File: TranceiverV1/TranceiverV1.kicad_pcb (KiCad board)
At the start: 2 copper layers, 2 parts, among them J1 Conn_01x02_Socket, U1 ESP32-WROOM-32E

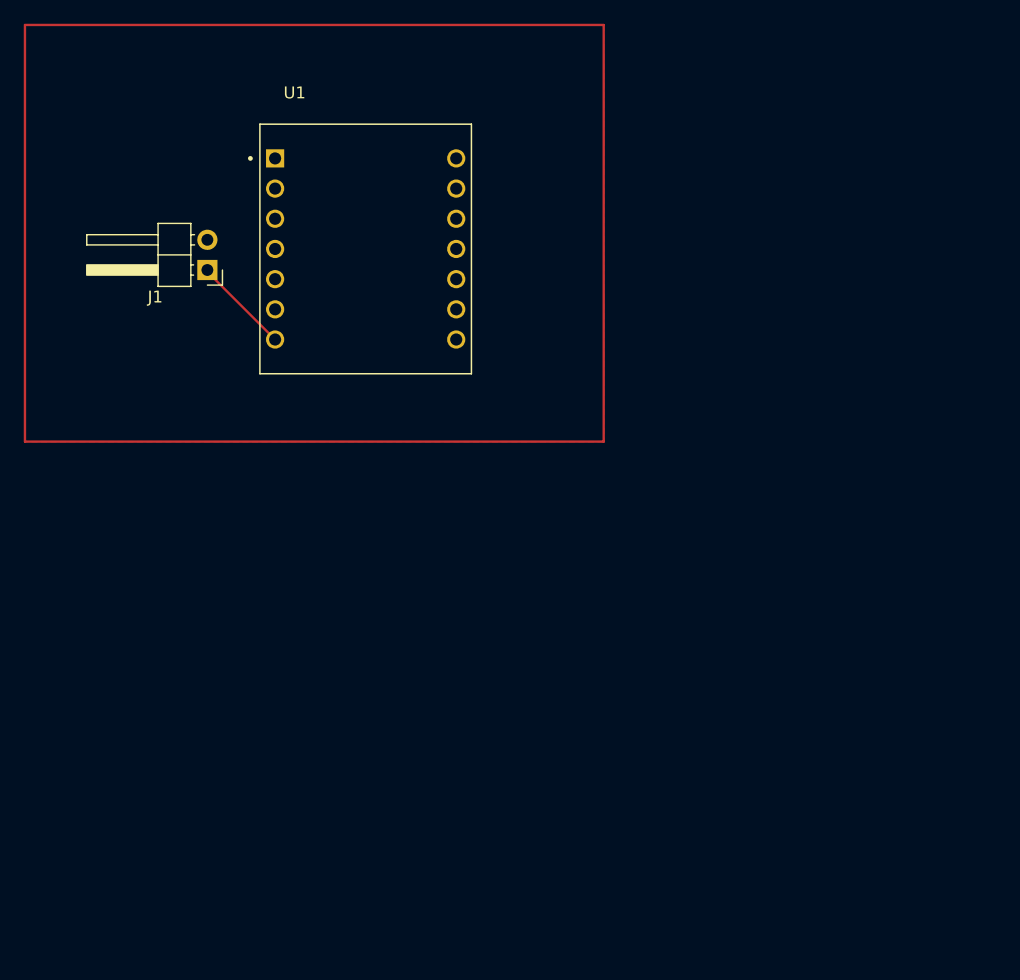
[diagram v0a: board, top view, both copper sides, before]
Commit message: arduino XIAO footprint and symbol added
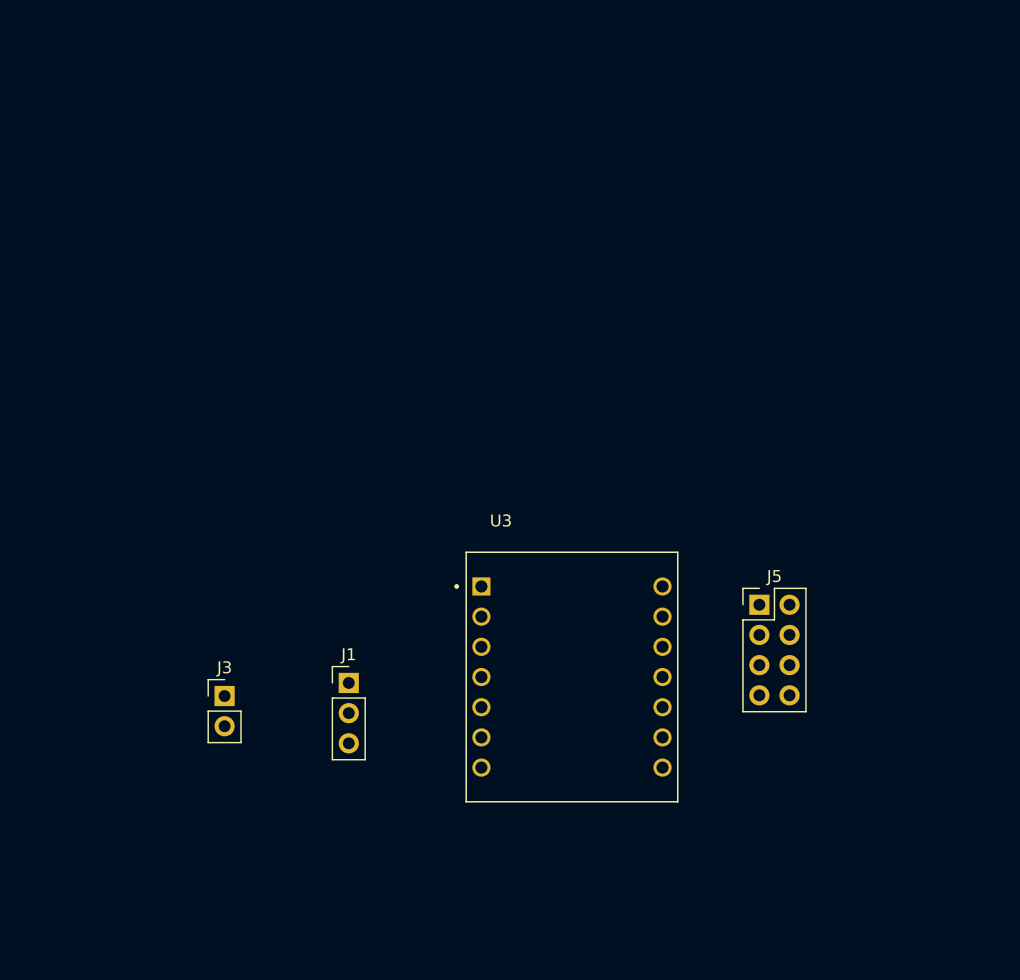
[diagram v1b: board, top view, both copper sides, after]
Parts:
- removed U1: ESP32-WROOM-32E, ArduinoXIAO:MODULE_102010388
- added J3: Conn_01x02_Socket, Connector_PinHeader_2.54mm:PinHeader_1x02_P2.54mm_Vertical, F.Cu at (144.7, 126.6)
- added J5: Conn_02x04_Odd_Even, Connector_PinHeader_2.54mm:PinHeader_2x04_P2.54mm_Vertical, F.Cu at (189.7, 118.9)
- added U3: 102010388, ArduinoXIAO:MODULE_102010388, F.Cu at (174.0, 125.0)
- J1: value Conn_01x02_Socket -> Conn_01x03_Socket; footprint Connector_PinHeader_2.54mm:PinHeader_1x02_P2.54mm_Horizontal -> Connector_PinHeader_2.54mm:PinHeader_1x03_P2.54mm_Vertical
- moved J1 36.7 mm to (155.2, 125.5), turned to 0 degrees
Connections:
- J1 pad 1: Net-(J1-Pin_1) -> /SERVO_DATA
- J1 pad 2: GND -> Net-(J1-Pin_2)
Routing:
- net Net-(J1-Pin_1): track 8.21 -> 0.00 mm
- removed copper zone on F.Cu, net GND

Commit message: designed first iteration of pcb
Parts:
- moved J3 6.16 mm to (150.4, 124.2)
- moved J1 4.72 mm to (158.0, 121.7)
- moved J5 3.49 mm to (192.3, 121.3)
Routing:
- net /CE: track 0.00 -> 45.4 mm, vias 0 -> 1
- net /CS: track 0.00 -> 45.1 mm
- net /VCC: track 0.00 -> 35.2 mm
- net /MOSI: track 0.00 -> 32.2 mm, vias 0 -> 1
- net /MISO: track 0.00 -> 26.6 mm
- net /SCK: track 0.00 -> 12.2 mm
- net /SERVO_DATA: track 0.00 -> 11.9 mm
- net GND: track 0.00 -> 11.3 mm
- net Net-(J1-Pin_2): track 0.00 -> 7.61 mm
- added copper zone on B.Cu, net GND
- added copper zone on F.Cu, net GND
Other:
- board outline added: 76.7 x 44.5 mm
- board text added: "6V Power"
